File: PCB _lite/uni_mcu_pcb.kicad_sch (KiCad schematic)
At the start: 67 parts, among them J1 USB_C_Receptacle_USB2.0, J2 Conn_01x02_Male, J3 Conn_02x08_Odd_Even, J4 Conn_01x05_Female, J5 Conn_01x04_Female, Q1 Q_NPN_BCE, Q2 Q_NPN_BCE, Q3 Q_NPN_BCE, Q4 Q_NPN_BCE, Q5 F7313, Q6 F7313, SW1 SW_DIP_x01, SW2 SW_DIP_x01, U1 CC56-12CGKWA, U2 CH330N, U4 STM32F030K6Tx, U5 LD1117S33TR_SOT223, Y1 8 Mhz

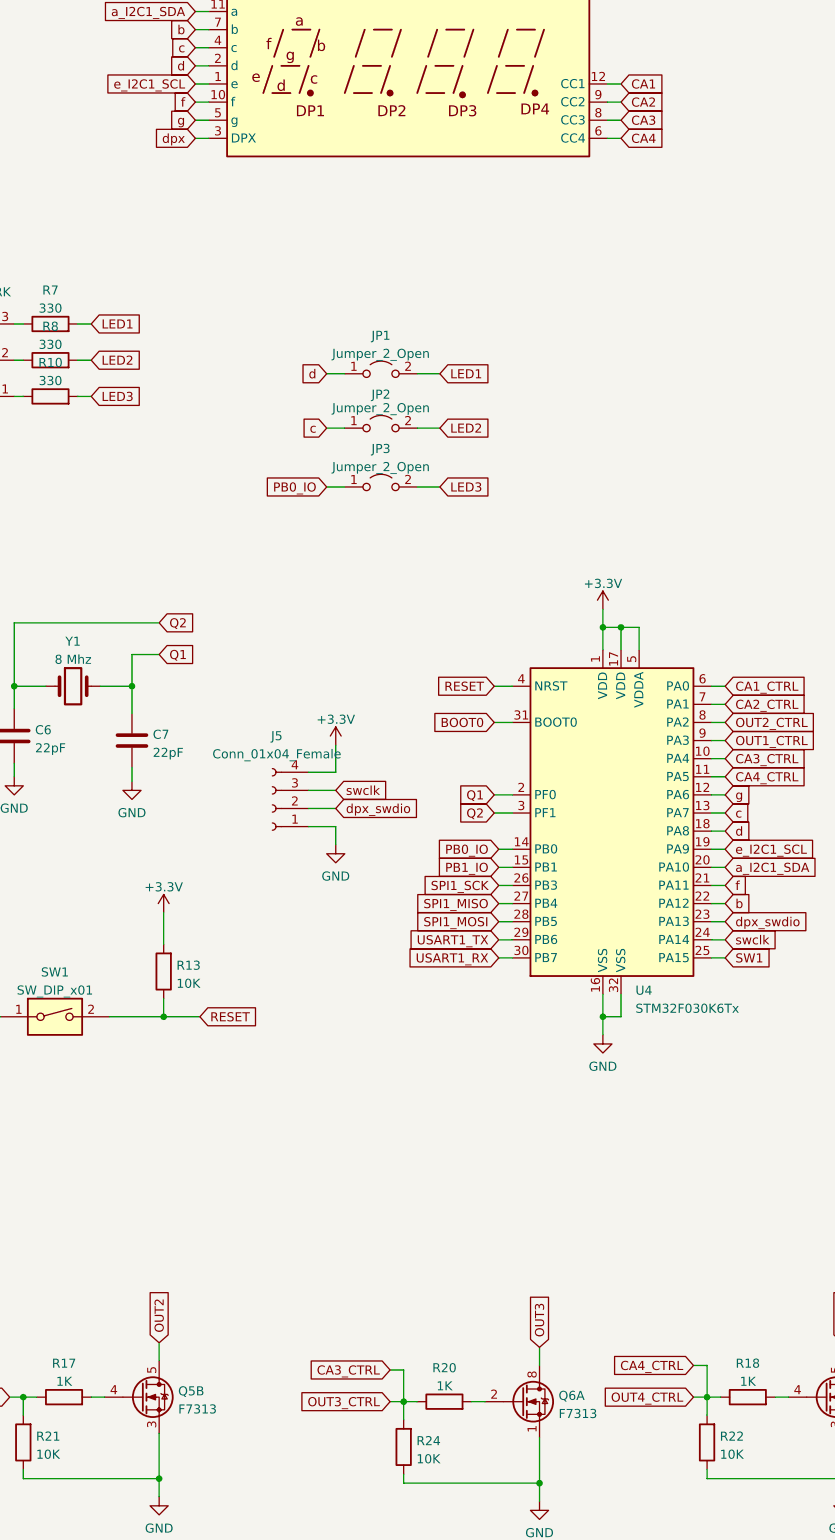
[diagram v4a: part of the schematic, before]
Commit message: Отредактирована распиновка, доделана шелкография
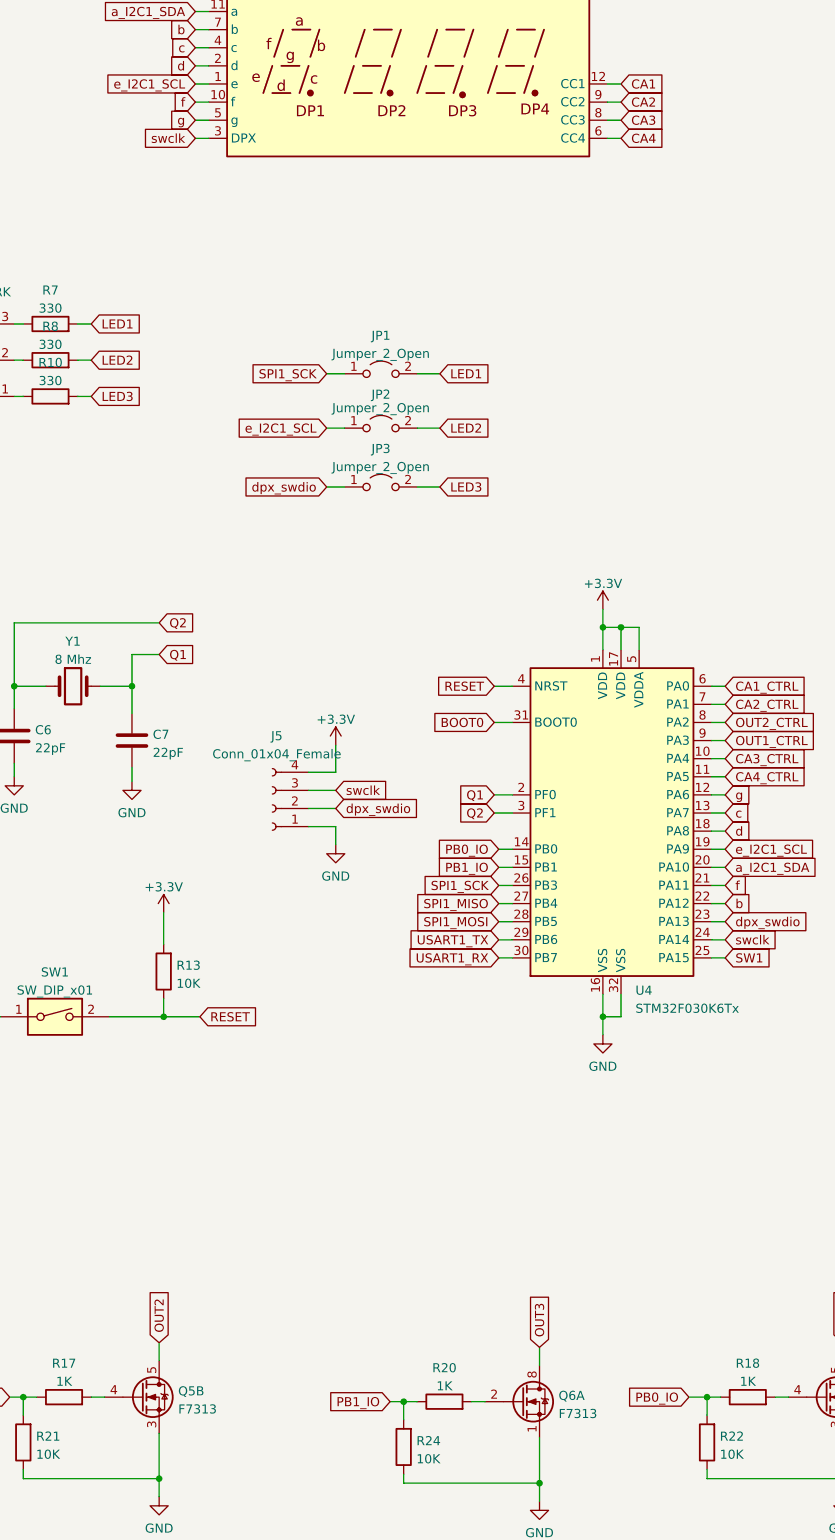
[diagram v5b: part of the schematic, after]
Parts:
- SW1, SW2: footprint Button_Switch_SMD:SW_Push_1P1T_NO_Vertical_Wuerth_434133025816 -> Button_Switch_SMD:SW_SPST_CK_RS282G05A3
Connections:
- net dpx is gone; now on net swclk: U1.3 (DPX)
- net CA3_CTRL: no longer R20.1, R24.2
- net CA4_CTRL: no longer R18.1, R22.2
- net PB0_IO: now also R18.1, R22.2; no longer JP3.1 (A)
- net PB1_IO: now also R20.1, R24.2
- net SPI1_SCK: now also JP1.1 (A)
- net c: no longer JP2.1 (A)
- net d: no longer JP1.1 (A)
- net dpx_swdio: now also JP3.1 (A)
- net e_I2C1_SCL: now also JP2.1 (A)
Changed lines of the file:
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@@
     (stroke (width 0) (type default) (color 0 0 0 0))
   )
-  (wire (pts (xy 340.36 224.155) (xy 340.36 228.6))
-    (stroke (width 0) (type default) (color 0 0 0 0))
-  )
   (wire (pts (xy 146.05 32.385) (xy 146.05 33.655))
     (stroke (width 0) (type default) (color 0 0 0 0))
@@
     (stroke (width 0) (type default) (color 0 0 0 0))
   )
-  (wire (pts (xy 295.91 224.79) (xy 297.815 224.79))
-    (stroke (width 0) (type default) (color 0 0 0 0))
-  )
   (wire (pts (xy 73.025 156.21) (xy 73.025 147.955))
     (stroke (width 0) (type default) (color 0 0 0 0))
@@
     (stroke (width 0) (type default) (color 0 0 0 0))
   )
-  (wire (pts (xy 338.455 228.6) (xy 340.36 228.6))
+  (wire (pts (xy 337.82 228.6) (xy 340.36 228.6))
     (stroke (width 0) (type default) (color 0 0 0 0))
   )
@@
     (stroke (width 0) (type default) (color 0 0 0 0))
   )
-  (wire (pts (xy 297.815 224.79) (xy 297.815 229.235))
-    (stroke (width 0) (type default) (color 0 0 0 0))
-  )
   (wire (pts (xy 52.705 98.425) (xy 54.61 98.425))
     (stroke (width 0) (type default) (color 0 0 0 0))
@@
     (stroke (width 0) (type default) (color 0 0 0 0))
   )
-  (wire (pts (xy 338.455 224.155) (xy 340.36 224.155))
-    (stroke (width 0) (type default) (color 0 0 0 0))
-  )
   (wire (pts (xy 83.82 109.22) (xy 85.09 109.22))
     (stroke (width 0) (type default) (color 0 0 0 0))
@@
     )
   )
+  (global_label "PB1_IO" (shape input) (at 295.91 229.235 180) (fields_autoplaced)
+    (effects (font (size 1.27 1.27)) (justify right))
+    (property "Intersheet References" "${INTERSHEET_REFS}" (id 0) (at 286.8445 229.1556 0)
+      (effects (font (size 1.27 1.27)) (justify right) hide)
+    )
+  )
   (global_label "c" (shape input) (at 342.9 146.685 0) (fields_autoplaced)
     (effects (font (size 1.27 1.27)) (justify left))
@@
     )
   )
-  (global_label "CA3_CTRL" (shape input) (at 295.91 224.79 180) (fields_autoplaced)
+  (global_label "dpx_swdio" (shape input) (at 287.02 100.965 180) (fields_autoplaced)
     (effects (font (size 1.27 1.27)) (justify right))
-    (property "Intersheet References" "${INTERSHEET_REFS}" (id 0) (at 284.4255 224.7106 0)
+    (property "Intersheet References" "${INTERSHEET_REFS}" (id 0) (at 275.0517 101.0444 0)
       (effects (font (size 1.27 1.27)) (justify right) hide)
     )
@@
     )
   )
-  (global_label "CA4_CTRL" (shape input) (at 338.455 224.155 180) (fields_autoplaced)
-    (effects (font (size 1.27 1.27)) (justify right))
-    (property "Intersheet References" "${INTERSHEET_REFS}" (id 0) (at 326.9705 224.0756 0)
-      (effects (font (size 1.27 1.27)) (justify right) hide)
-    )
-  )
   (global_label "d" (shape input) (at 268.605 41.91 180) (fields_autoplaced)
     (effects (font (size 1.27 1.27)) (justify right))
@@
     )
   )
-  (global_label "d" (shape input) (at 287.02 85.09 180) (fields_autoplaced)
-    (effects (font (size 1.27 1.27)) (justify right))
-    (property "Intersheet References" "${INTERSHEET_REFS}" (id 0) (at 283.4579 85.1694 0)
-      (effects (font (size 1.27 1.27)) (justify right) hide)
-    )
-  )
   (global_label "OUT4" (shape input) (at 359.41 220.98 90) (fields_autoplaced)
     (effects (font (size 1.27 1.27)) (justify left))
@@
     )
   )
+  (global_label "PB0_IO" (shape input) (at 337.82 228.6 180) (fields_autoplaced)
+    (effects (font (size 1.27 1.27)) (justify right))
+    (property "Intersheet References" "${INTERSHEET_REFS}" (id 0) (at 328.7545 228.5206 0)
+      (effects (font (size 1.27 1.27)) (justify right) hide)
+    )
+  )
   (global_label "CA1_CTRL" (shape input) (at 342.9 128.905 0) (fields_autoplaced)
     (effects (font (size 1.27 1.27)) (justify left))
@@
     )
   )
-  (global_label "PB0_IO" (shape input) (at 287.02 100.965 180) (fields_autoplaced)
-    (effects (font (size 1.27 1.27)) (justify right))
-    (property "Intersheet References" "${INTERSHEET_REFS}" (id 0) (at 277.9545 100.8856 0)
-      (effects (font (size 1.27 1.27)) (justify right) hide)
-    )
-  )
   (global_label "g" (shape input) (at 342.9 144.145 0) (fields_autoplaced)
     (effects (font (size 1.27 1.27)) (justify left))
@@
     )
   )
-  (global_label "OUT3_CTRL" (shape input) (at 295.91 229.235 180) (fields_autoplaced)
-    (effects (font (size 1.27 1.27)) (justify right))
-    (property "Intersheet References" "${INTERSHEET_REFS}" (id 0) (at 283.1555 229.1556 0)
-      (effects (font (size 1.27 1.27)) (justify right) hide)
-    )
-  )
   (global_label "SW1" (shape input) (at 156.21 218.44 0) (fields_autoplaced)
     (effects (font (size 1.27 1.27)) (justify left))
@@
     )
   )
+  (global_label "e_I2C1_SCL" (shape input) (at 287.02 92.71 180) (fields_autoplaced)
+    (effects (font (size 1.27 1.27)) (justify right))
+    (property "Intersheet References" "${INTERSHEET_REFS}" (id 0) (at 273.7817 92.7894 0)
+      (effects (font (size 1.27 1.27)) (justify right) hide)
+    )
+  )
   (global_label "e_I2C1_SCL" (shape input) (at 268.605 44.45 180) (fields_autoplaced)
     (effects (font (size 1.27 1.27)) (justify right))
@@
     )
   )
-  (global_label "dpx" (shape input) (at 268.605 52.07 180) (fields_autoplaced)
+  (global_label "swclk" (shape input) (at 268.605 52.07 180) (fields_autoplaced)
     (effects (font (size 1.27 1.27)) (justify right))
-    (property "Intersheet References" "${INTERSHEET_REFS}" (id 0) (at 262.8657 51.9906 0)
+    (property "Intersheet References" "${INTERSHEET_REFS}" (id 0) (at 261.0514 51.9906 0)
       (effects (font (size 1.27 1.27)) (justify right) hide)
     )
@@
     )
   )
-  (global_label "OUT4_CTRL" (shape input) (at 338.455 228.6 180) (fields_autoplaced)
-    (effects (font (size 1.27 1.27)) (justify right))
-    (property "Intersheet References" "${INTERSHEET_REFS}" (id 0) (at 325.7005 228.5206 0)
-      (effects (font (size 1.27 1.27)) (justify right) hide)
-    )
-  )
   (global_label "OUT1" (shape input) (at 373.38 192.405 180) (fields_autoplaced)
     (effects (font (size 1.27 1.27)) (justify right))
@@
     )
   )
-  (global_label "c" (shape input) (at 287.02 92.71 180) (fields_autoplaced)
-    (effects (font (size 1.27 1.27)) (justify right))
-    (property "Intersheet References" "${INTERSHEET_REFS}" (id 0) (at 283.5183 92.7894 0)
-      (effects (font (size 1.27 1.27)) (justify right) hide)
-    )
-  )
   (global_label "c" (shape input) (at 268.605 39.37 180) (fields_autoplaced)
     (effects (font (size 1.27 1.27)) (justify right))
@@
     )
   )
+  (global_label "SPI1_SCK" (shape input) (at 287.02 85.09 180) (fields_autoplaced)
+    (effects (font (size 1.27 1.27)) (justify right))
+    (property "Intersheet References" "${INTERSHEET_REFS}" (id 0) (at 275.5959 85.0106 0)
+      (effects (font (size 1.27 1.27)) (justify right) hide)
+    )
+  )
   (global_label "g" (shape input) (at 268.605 49.53 180) (fields_autoplaced)
     (effects (font (size 1.27 1.27)) (justify right))
@@
     (property "Reference" "SW2" (id 0) (at 135.89 212.2002 0))
     (property "Value" "SW_DIP_x01" (id 1) (at 135.89 214.7371 0))
-    (property "Footprint" "Button_Switch_SMD:SW_Push_1P1T_NO_Vertical_Wuerth_434133025816" (id 2) (at 135.89 218.44 0)
+    (property "Footprint" "Button_Switch_SMD:SW_SPST_CK_RS282G05A3" (id 2) (at 135.89 218.44 0)
       (effects (font (size 1.27 1.27)) hide)
     )
@@
     (pin "7")
     (pin "8")
-    (pin "3")
-    (pin "4")
-    (pin "5")
-    (pin "6")
   )
   (symbol (lib_id "power:GND") (at 112.395 45.085 0) (unit 1)
@@
     (property "Reference" "SW1" (id 0) (at 248.92 169.0202 0))
     (property "Value" "SW_DIP_x01" (id 1) (at 248.92 171.5571 0))
-    (property "Footprint" "Button_Switch_SMD:SW_Push_1P1T_NO_Vertical_Wuerth_434133025816" (id 2) (at 248.92 175.26 0)
+    (property "Footprint" "Button_Switch_SMD:SW_SPST_CK_RS282G05A3" (id 2) (at 248.92 175.26 0)
       (effects (font (size 1.27 1.27)) hide)
     )
@@
       (effects (font (size 1.27 1.27)) (justify left) hide)
     )
-    (pin "1")
-    (pin "2")
-    (pin "7")
-    (pin "8")
     (pin "3")
     (pin "4")
@@
     (pin "7")
     (pin "8")
-    (pin "3")
-    (pin "4")
-    (pin "5")
-    (pin "6")
   )
   (symbol (lib_id "Simulation_SPICE:DIODE") (at 66.04 147.955 0) (unit 1)
@@
       (effects (font (size 1.27 1.27)) (justify left) hide)
     )
-    (pin "1")
-    (pin "2")
-    (pin "7")
-    (pin "8")
     (pin "3")
     (pin "4")
@@
     )
     (path "/6b606e4d-2846-457e-994b-dea58630801e"
-      (reference "SW1") (unit 1) (value "SW_DIP_x01") (footprint "Button_Switch_SMD:SW_Push_1P1T_NO_Vertical_Wuerth_434133025816")
+      (reference "SW1") (unit 1) (value "SW_DIP_x01") (footprint "Button_Switch_SMD:SW_SPST_CK_RS282G05A3")
     )
     (path "/297f56ba-9aac-4f73-8194-d97a978b5443"
-      (reference "SW2") (unit 1) (value "SW_DIP_x01") (footprint "Button_Switch_SMD:SW_Push_1P1T_NO_Vertical_Wuerth_434133025816")
+      (reference "SW2") (unit 1) (value "SW_DIP_x01") (footprint "Button_Switch_SMD:SW_SPST_CK_RS282G05A3")
     )
     (path "/8345b1ee-959e-4a4c-b0a7-eeb665eae99b"

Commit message: Схема теперь А4, Сформированы герберы
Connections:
- no-connect marks 1 -> 3
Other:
- title: (none) -> Ну вот нахуя я А3 в А4 пихнул, блять
- moved on the sheet: C1, C10, C2, C3, C4, C5, C6, C7, C8, C9, D1, D2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
